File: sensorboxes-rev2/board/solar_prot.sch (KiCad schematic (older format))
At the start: 11 parts

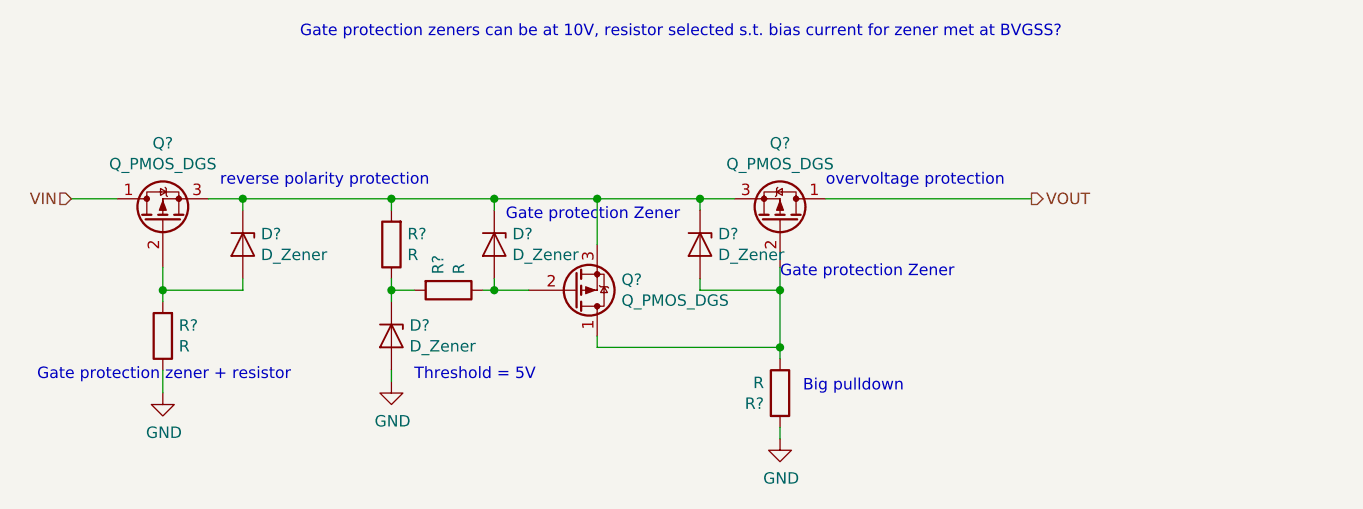
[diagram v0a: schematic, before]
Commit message: developed more of the schematic for the STM32 + radio. also picked out passives & figured out bidirectional battery polarity checking + reverse polarity protection for the solar panel.
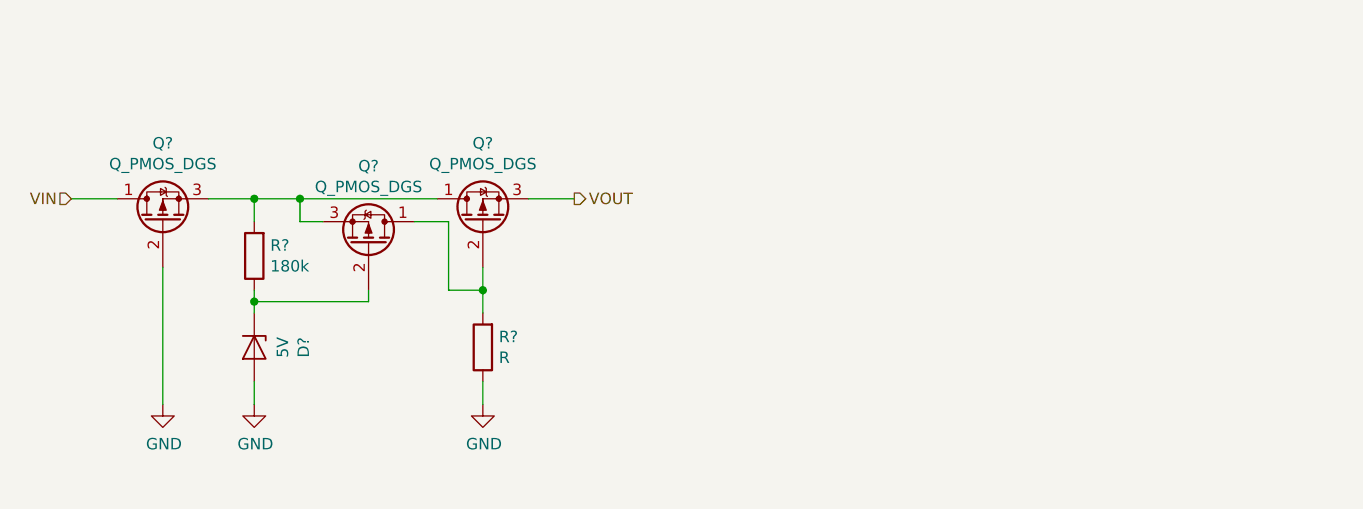
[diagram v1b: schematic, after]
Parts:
- removed D? (x4): D_Zener, symbol Device:D_Zener
- removed Q? (x3): Q_PMOS_DGS, symbol Device:Q_PMOS_DGS
- removed R? (x4): R, symbol Device:R
- added D?: 5V, symbol Device:D_Zener
- added Q? (x3): Q_PMOS_DGS, symbol Device:Q_PMOS_DGS
- added R?: 180k, symbol Device:R
- added R?: R, symbol Device:R
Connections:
- net GND: now also D?.2 (A), Q?.2 (G), R?.1
- net VIN: now also Q?.1 (D)
- net VOUT: now also Q?.3 (S)
- new net: Q?.1 (D), Q?.3 (S), Q?.3 (S), R?.2
- new net: Q?.1 (D), Q?.2 (G), R?.2
- new net: D?.1 (K), Q?.2 (G), R?.1
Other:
- note removed: "Big pulldown"
- note removed: "Gate protection Zener"
- note removed: "Gate protection zener + resistor"
- note removed: "Gate protection zeners can be at 10V, resistor selected s.t. bias current for zener met at BVGSS?"
- note removed: "Threshold = 5V\n"
- note removed: "overvoltage protection"
- note removed: "reverse polarity protection"
